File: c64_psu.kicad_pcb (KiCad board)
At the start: 2 copper layers, 111.4 x 70.6 mm, 39 parts, among them J1 230VAC, J2 230VAC, J5 5VDC, J6 GND, J7 12VDC, J8 GND, Q1 BT145, Q2 BT145, U1 LM2596S-ADJ, U2 LM2596S-ADJ

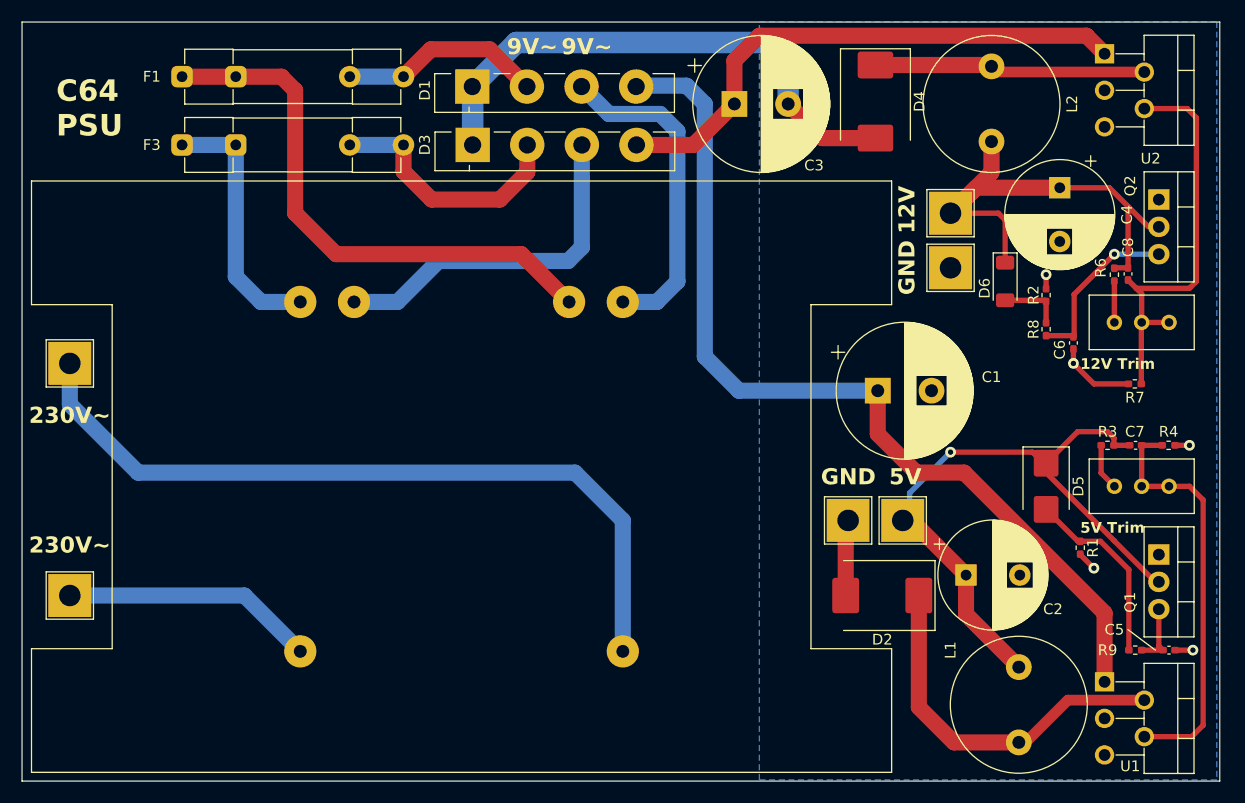
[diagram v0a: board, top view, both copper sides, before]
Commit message: v2.0: Replace LM2596 with SMD type
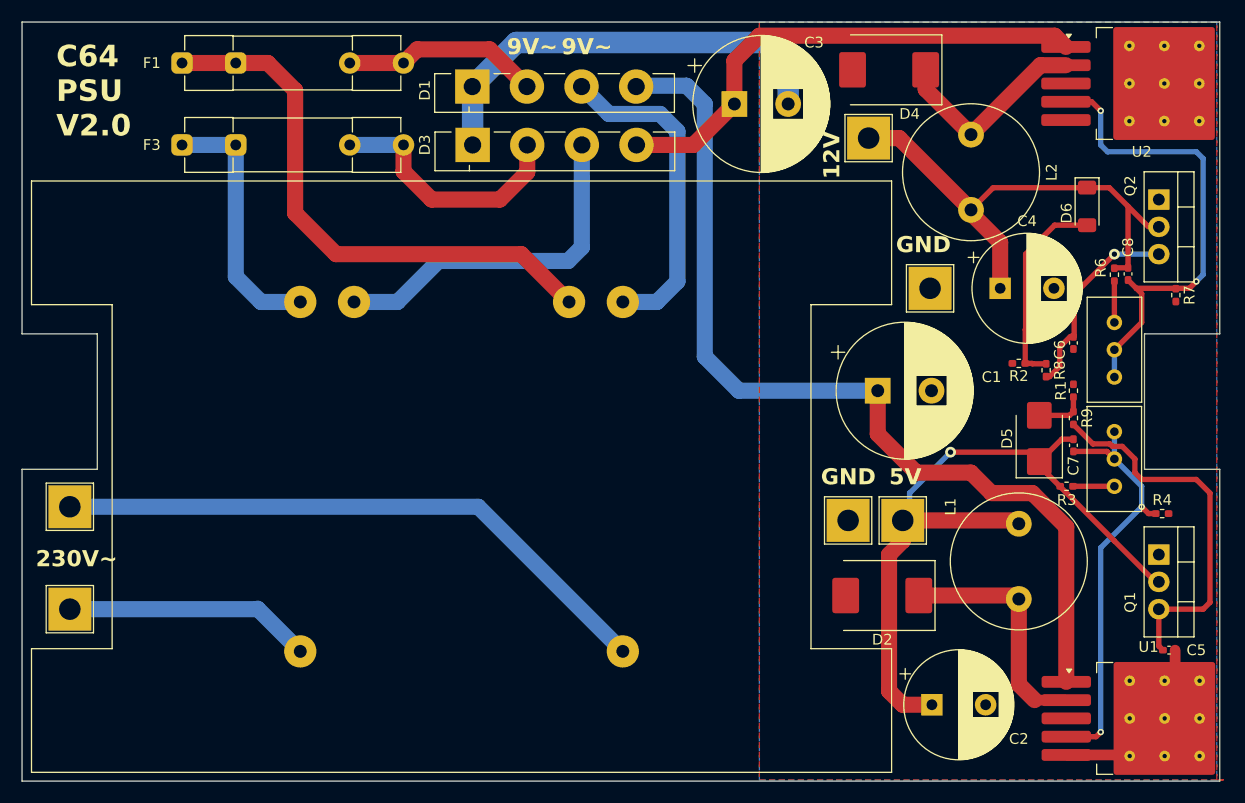
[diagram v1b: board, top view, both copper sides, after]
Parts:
- U1, U2: footprint Package_TO_SOT_THT:TO-220-5_P3.4x3.7mm_StaggerOdd_Lead3.8mm_Vertical -> c64_psu:TO-263-5_TabPin3
- moved R9 22.3 mm to (171.4, 81.3), turned to 90 degrees
- moved R1 14.6 mm to (171.4, 78.7), turned to 90 degrees
- moved L1 13.3 mm to (166.4, 98.1)
- moved J1 13.3 mm to (78.1, 89.5)
- moved C2 12.5 mm to (158.3, 108.0)
- moved C4 10.9 mm to (164.6, 69.2), turned to 0 degrees
- moved D6 10.3 mm to (172.7, 61.6)
- moved J7 10.3 mm to (152.4, 55.2)
- moved R7 9.09 mm to (181.0, 69.8), turned to -90 degrees
- moved R2 6.84 mm to (166.4, 76.2), turned to 180 degrees
- moved L2 6.63 mm to (161.9, 54.9)
- moved R4 6.38 mm to (179.7, 90.2)
- moved C7 5.78 mm to (171.4, 83.8), turned to -90 degrees
- moved R3 5.39 mm to (170.8, 87.6), turned to 0 degrees
- moved U1 5.32 mm to (178.4, 109.2), turned to 0 degrees
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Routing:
- net Net-(Q1-G): track 5.94 -> 35.2 mm
- net Net-(J1-Pin_1): track 71.9 -> 57.0 mm
- net Net-(D6-A): track 5.84 -> 19.0 mm
- net Net-(D5-A): track 17.5 -> 5.27 mm
- net Net-(D2-K): track 33.7 -> 22.4 mm
- net GND: track 72.5 -> 61.6 mm, vias 5 -> 0
- net /5VDC: track 60.9 -> 68.9 mm
- net Net-(D4-K): track 25.3 -> 19.3 mm
- net /FB12V: track 39.0 -> 44.9 mm, vias 0 -> 2
- net Net-(D3-+): track 50.8 -> 46.9 mm
- net Net-(Q2-G): track 15.9 -> 18.5 mm
- net Net-(D1-+): track 86.4 -> 87.5 mm
- net /12VDC: track 45.5 -> 46.6 mm
- net /FB5V: track 38.8 -> 39.6 mm, vias 0 -> 2
- net Net-(F1-Pad1): track 51.4 -> 51.9 mm
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- added copper zone on F.Cu, net GND
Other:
- outline, holes or cut-outs redrawn
- board text added: "C64 PSU V2.0"
- board text removed: "12V Trim"
- board text removed: "5V Trim"
- board text removed: "C64 PSU"
